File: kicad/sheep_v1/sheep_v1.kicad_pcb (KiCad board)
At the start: 2 copper layers, 144.6 x 88.9 mm, 35 parts, among them J2 AudioJack4dpb, SW1 SW_Push, SW10 SW_Push, SW11 SW_Push, SW12 SW_Push, SW13 SW_Push, SW14 SW_Push, SW15 SW_Push, SW16 SW_Push, SW17 SW_Push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

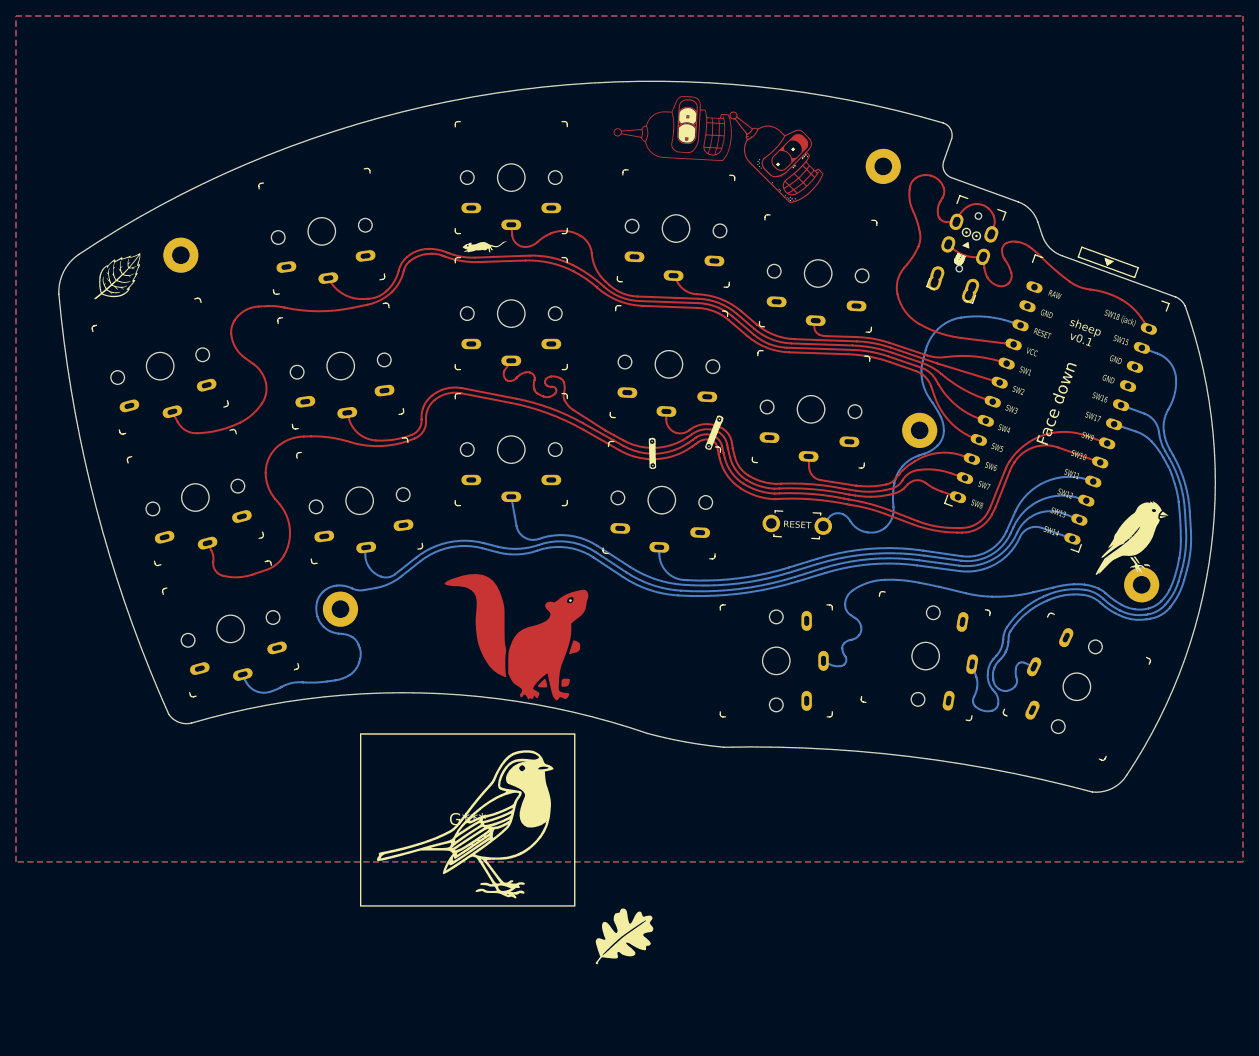
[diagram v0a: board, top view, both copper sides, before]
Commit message: Reversed controller ok + up matrix pins
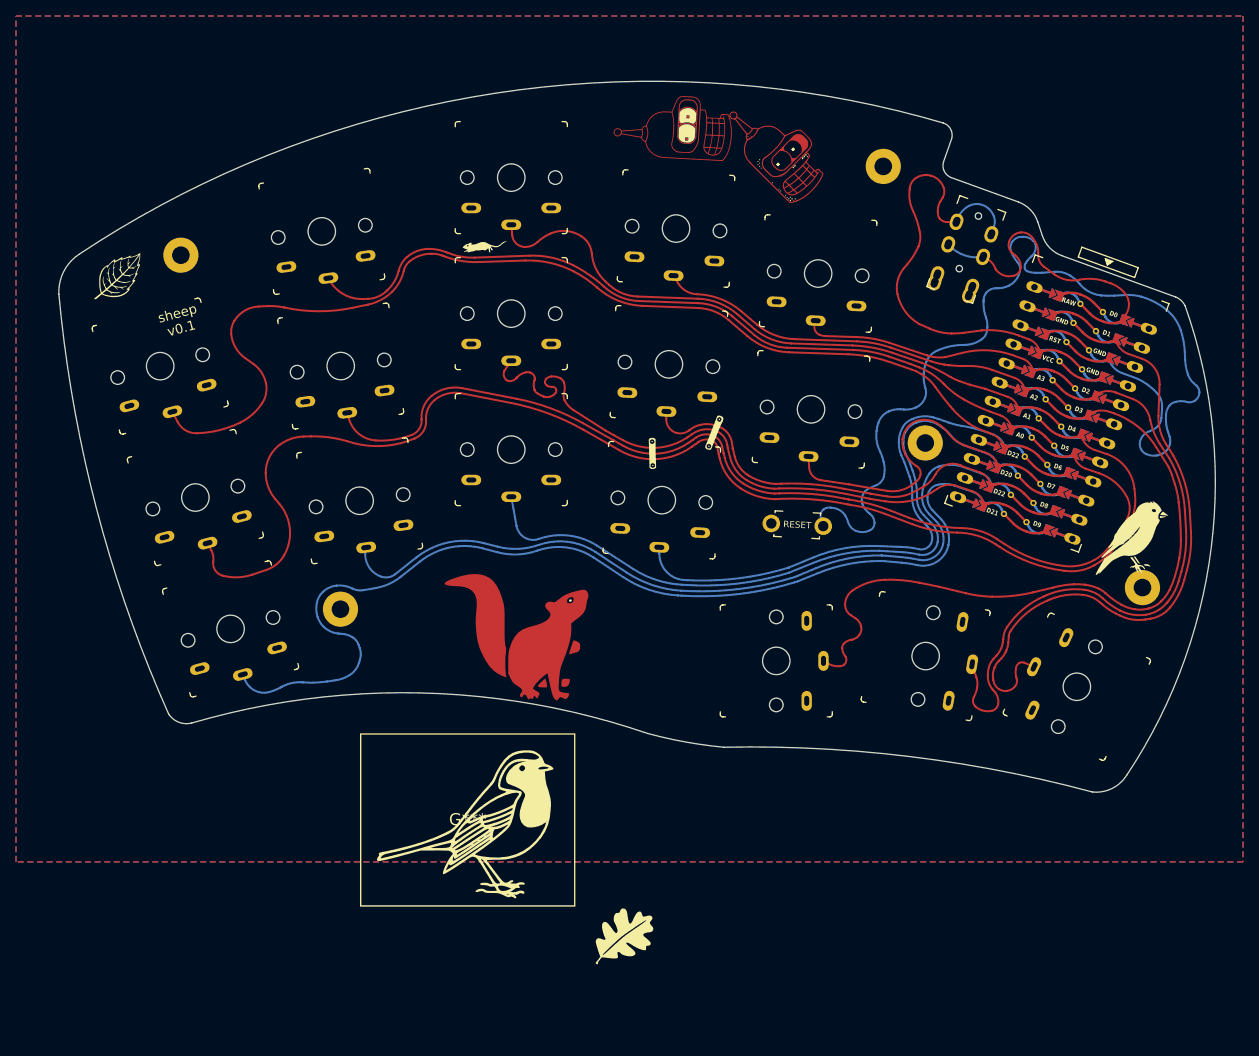
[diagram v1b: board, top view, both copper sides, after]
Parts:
- added G***: LOGO, LOGO, B.Cu at (153.4, 110.3)
- moved ? 1.72 mm to (151.8, 97.3)
- moved ? 0.36 mm to (178.9, 115.3)
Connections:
- U1 pad 7: Switch9 -> Switch10
- U1 pad 8: Switch10 -> Switch9
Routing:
- net reset: track 49.6 -> 128.2 mm
- net Switch10: track 147.3 -> 163.1 mm
- net Switch6: track 24.0 -> 37.8 mm
- net Switch9: track 112.9 -> 124.7 mm
- net Switch12: track 80.8 -> 89.1 mm
- net Switch11: track 61.6 -> 67.6 mm
- net Switch7: track 44.5 -> 49.5 mm
- net Switch3: track 69.9 -> 74.6 mm
- net Switch1: track 25.9 -> 30.3 mm
- net vcc: track 51.8 -> 56.2 mm
- net Switch16: track 70.9 -> 75.2 mm
- net Switch17: track 81.4 -> 85.6 mm
- net Switch2: track 44.0 -> 48.2 mm
- net Switch8: track 75.9 -> 79.9 mm
- net Switch4: track 92.2 -> 95.8 mm
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
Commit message: Reverse pads & up mergins
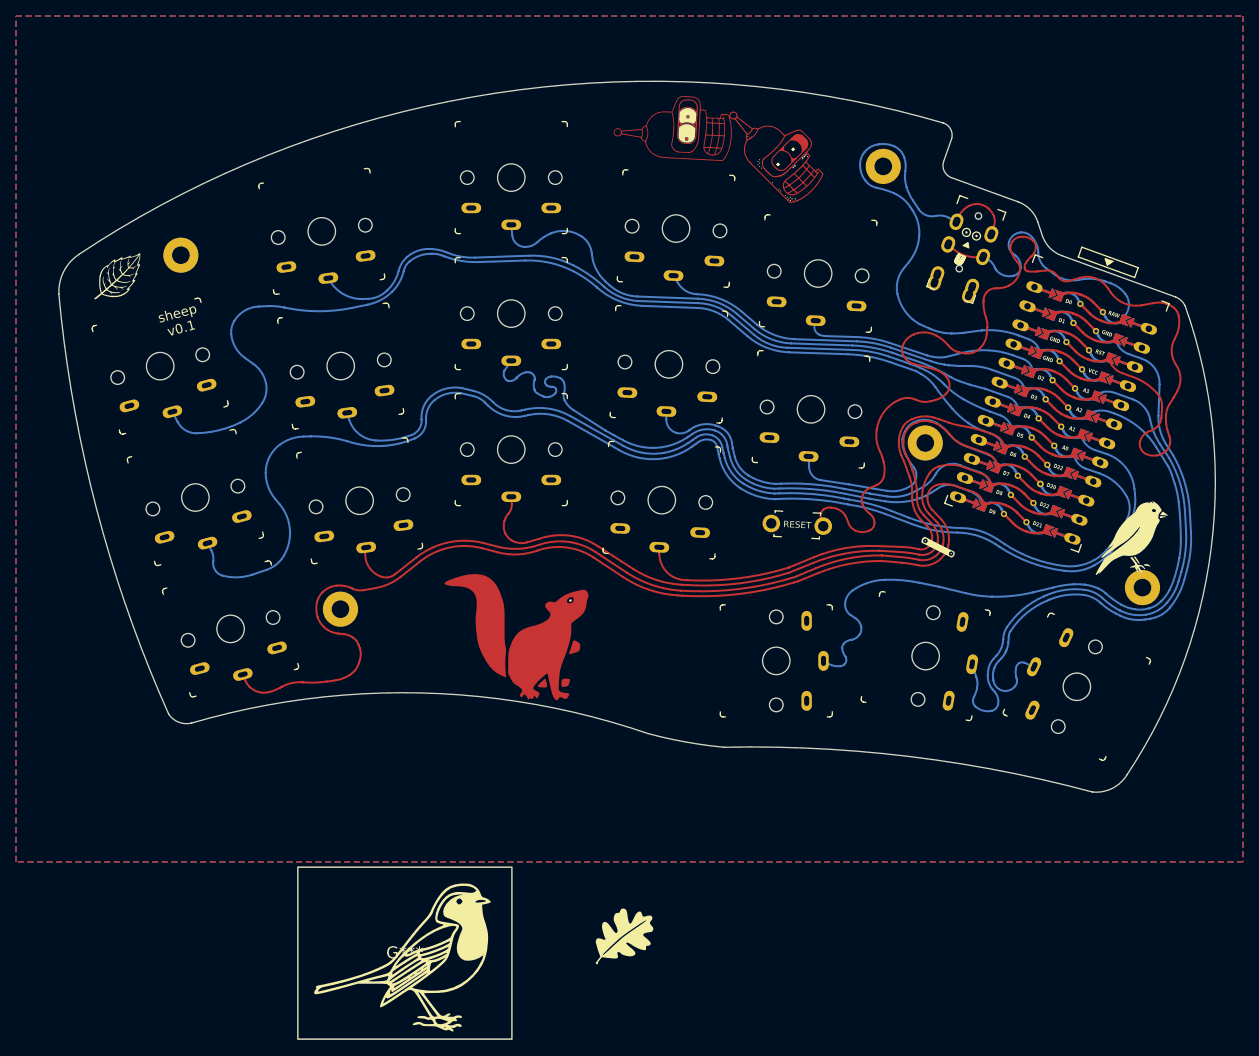
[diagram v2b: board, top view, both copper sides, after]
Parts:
- G*** (x3): moved to B.Cu
- G***: moved to F.Cu
- moved G*** 18.4 mm to (86.7, 161.0)
- moved G*** 0.98 mm to (97.7, 72.7), turned to 178 degrees
- moved G*** 0.10 mm to (125.3, 96.0), turned to 158 degrees
- turned G*** to 179 degrees
- turned G*** to 63 degrees
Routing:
- net vcc: track 56.2 -> 70.3 mm
- net reset: track 128.2 -> 139.2 mm
- net Switch12: track 89.1 -> 91.4 mm
- net Switch6: track 37.8 -> 37.1 mm
